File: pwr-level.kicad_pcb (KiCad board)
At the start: 2 copper layers, 45.7 x 30.5 mm, 15 parts, among them J1 Conn_01x02, J2 Conn_01x01, J3 Conn_01x01, U1 L78L05_SOT89, U2 ATtiny13-20SU, U3 MAX7219, U4 KCSA02-106, U5 KCSA02-106, U6 KCSA02-106

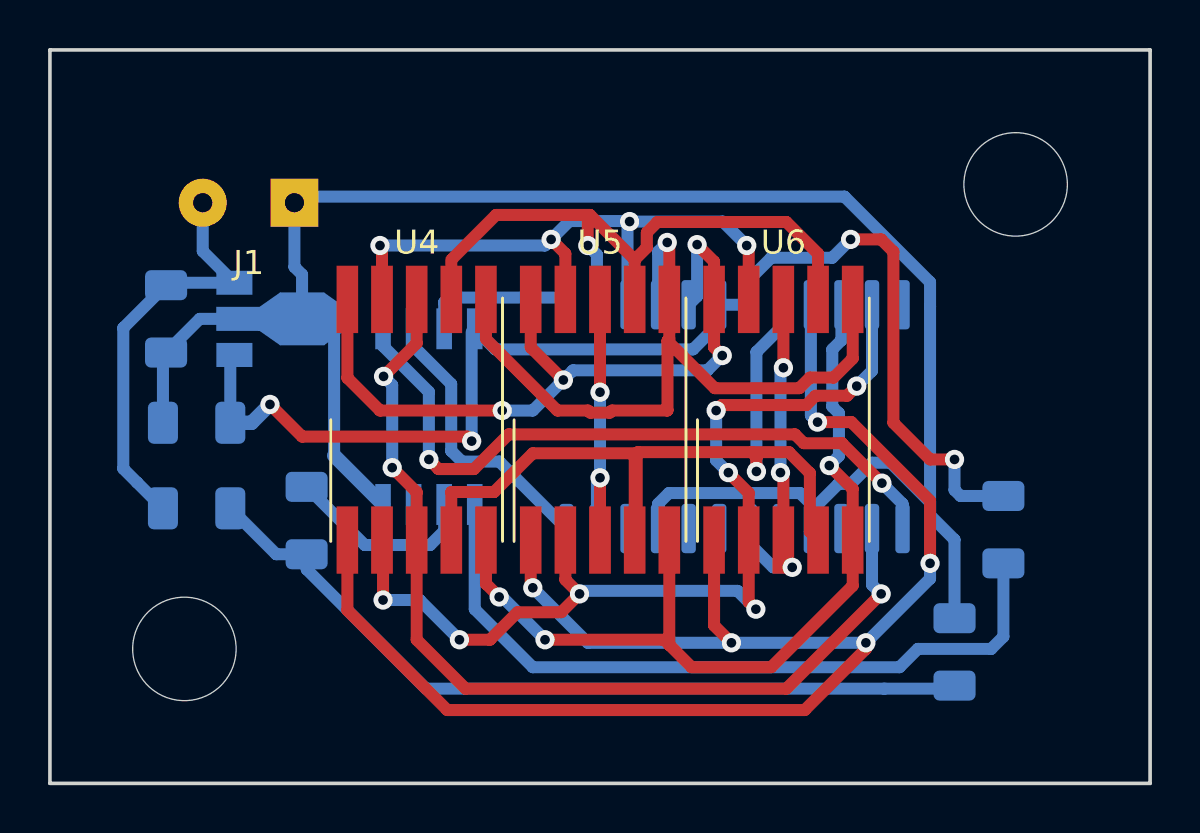
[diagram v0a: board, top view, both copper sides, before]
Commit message: Schematics/PCB update
- Added current limit resistor for LED display
- Updated PCB layout
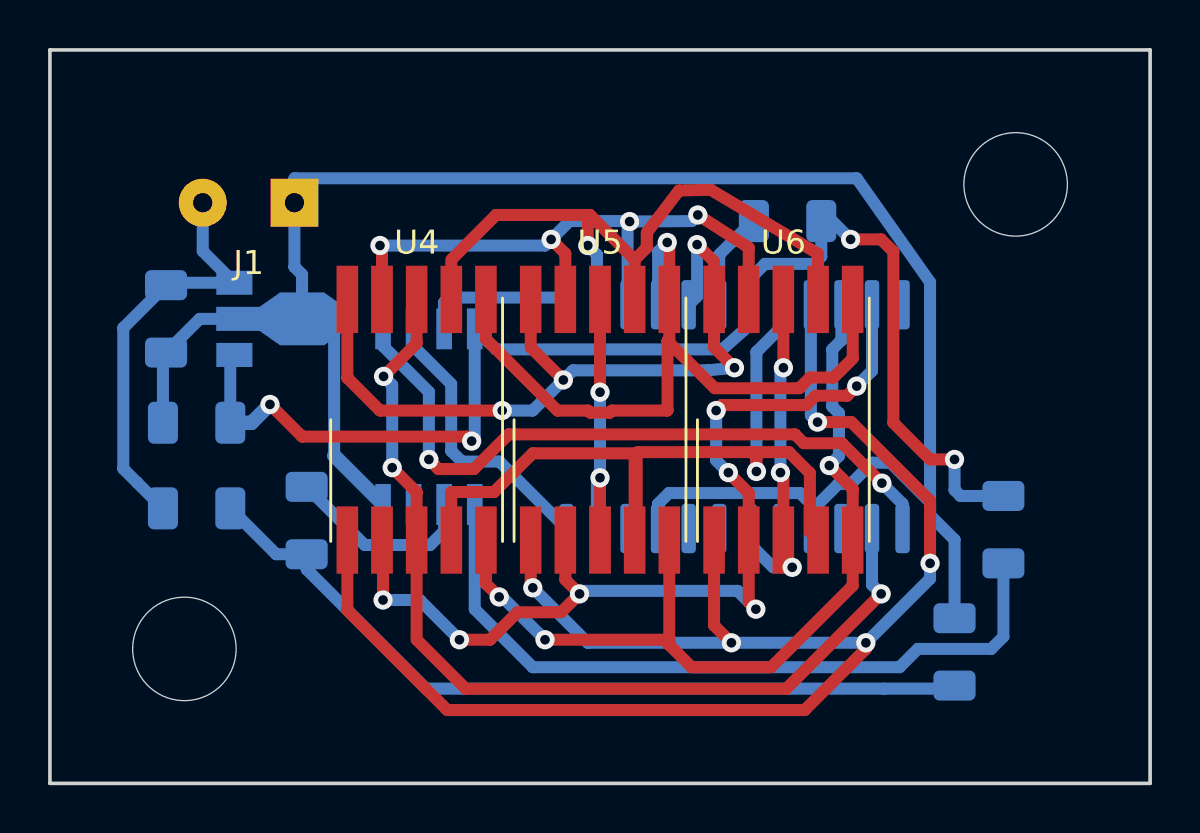
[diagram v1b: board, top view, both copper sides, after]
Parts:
- added R5: 1kOm, Resistor_SMD:R_1206_3216Metric, B.Cu at (172.9, 75.2)
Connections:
- U3 pad 18: +5V -> Net-(R5-Pad1)
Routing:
- net Net-(R5-Pad1): track 0.00 -> 3.99 mm
- net GND: track 83.4 -> 85.1 mm
- net +5V: track 53.2 -> 54.9 mm
- net /SEG_G: track 31.9 -> 32.9 mm
- net /SEG_A: track 27.5 -> 28.3 mm
- removed copper zone on B.Cu, net GND
- removed copper zone on F.Cu, net GND

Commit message: Schematics update
- Added 1pin markers for CPU/LED driver
- Updated b.Cu/f.Cu GND fill
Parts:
- R5: value 1kOm -> 10kOm
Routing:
- added copper zone on B.Cu, net GND
- added copper zone on F.Cu, net GND
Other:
- board text added: "."
